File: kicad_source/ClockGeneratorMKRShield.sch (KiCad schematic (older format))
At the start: 32 parts, among them CN1 ARDUINO_MKR, CN2 60312202114509, CN3 60312202114509, CN4 SM04B-SRSS-TB, U1 SI5351A, Y1 RH100-25.000-6-F-1010-TR

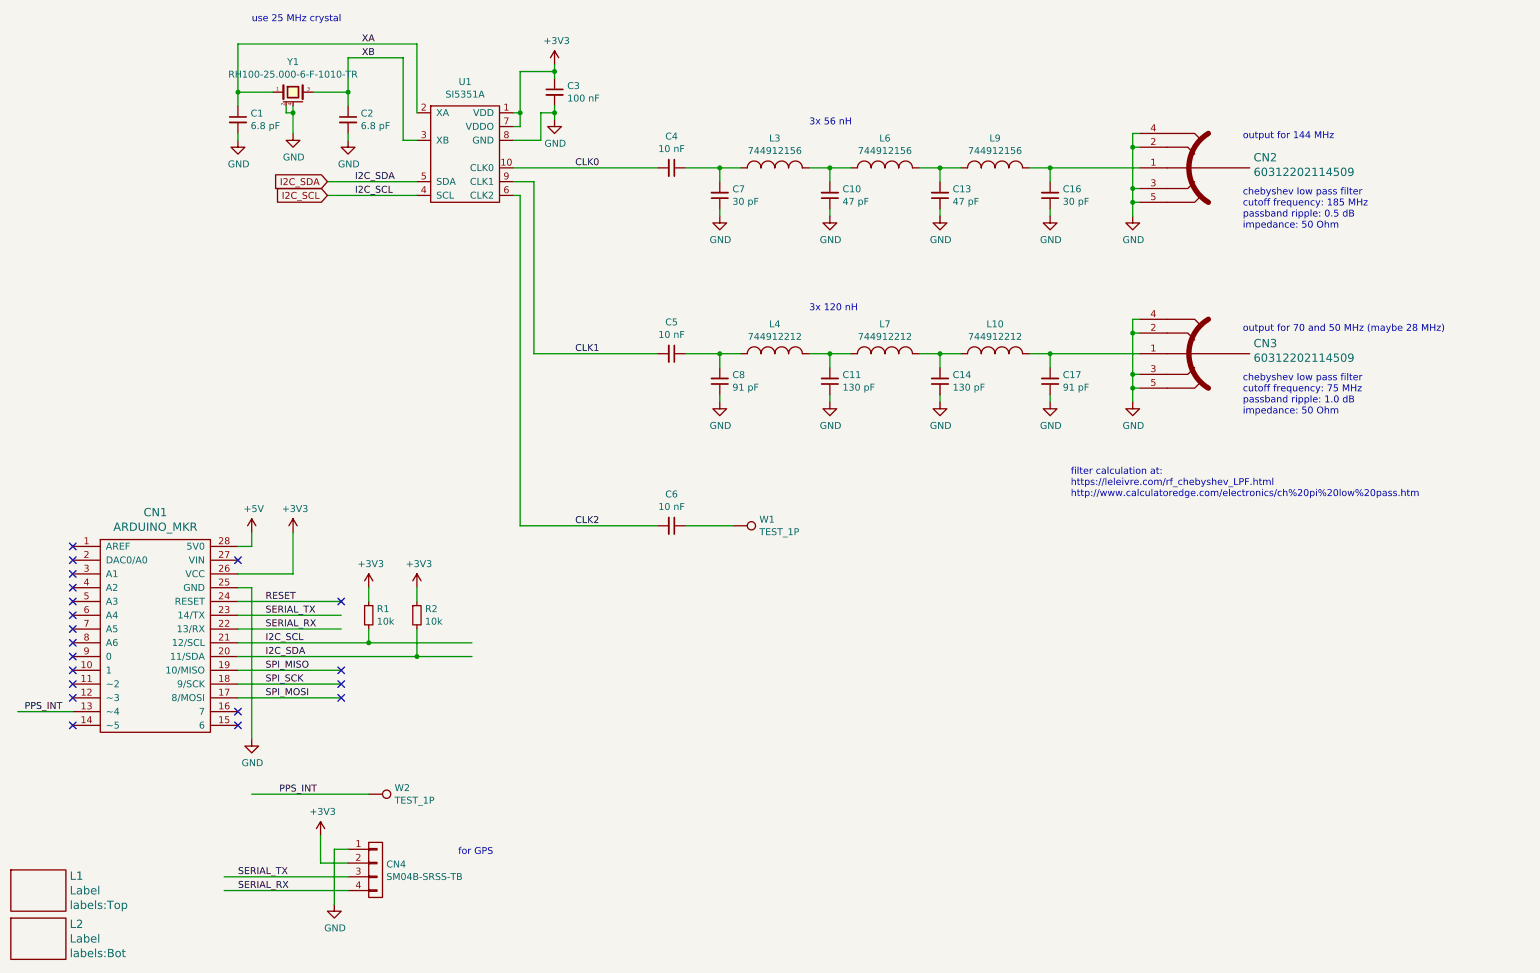
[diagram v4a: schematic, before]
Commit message: switched to clock generator in QFN package, updated layout
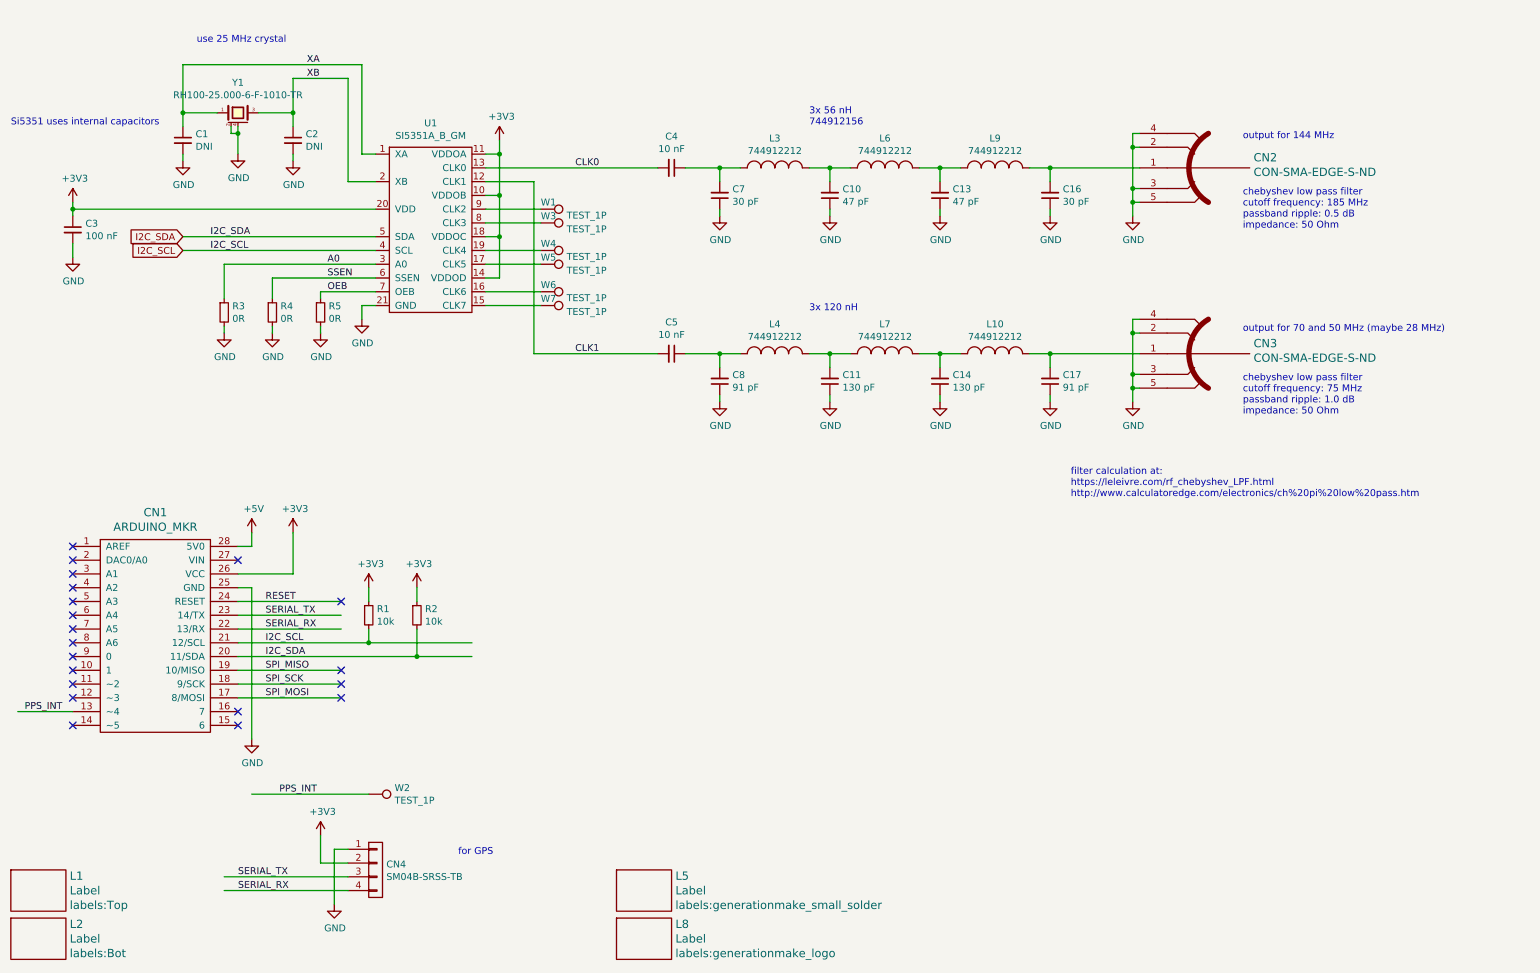
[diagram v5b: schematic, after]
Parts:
- removed C6: 10 nF, capacitors:C_0603, symbol devices:C_0603
- removed U1: SI5351A, SSOP:MSOP-10_3x3mm_Pitch0.5mm, symbol IC_interface_i2c:SI5351A
- added L5: Label, labels:generationmake_small_solder, symbol devices:Label
- added L8: Label, labels:generationmake_logo, symbol devices:Label
- added R3, R4, R5: 0R, resistors:R_0603, symbol devices:R_0603
- added U1: SI5351A_B_GM, QFN:QFN-20-1EP_4x4mm_P0.5mm_EP2.5x2.5mm, symbol IC_interface_i2c:SI5351A_B_GM
- added W3, W4, W5, W6, W7: TEST_1P, wire_pads:SolderWirePad_single_1mmSMD, symbol mechanical-connectors:TEST_1P
- C1, C2: value 6.8 pF -> DNI
- CN2, CN3: value 60312202114509 -> CON-SMA-EDGE-S-ND
- L3, L6, L9: value 744912156 -> 744912212
- W1: footprint wire_pads:SolderWirePad_single_0-8mmDrill -> wire_pads:SolderWirePad_single_1mmSMD
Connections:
- net labels added: A0, OEB, SSEN
- net labels removed: CLK2
- wire segments 115 -> 129
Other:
- note added: "3x 56 nH\n744912156"
- note added: "Si5351 uses internal capacitors"
- note removed: "3x 56 nH"
- moved on the sheet: C1, C2, C3, W1, Y1
